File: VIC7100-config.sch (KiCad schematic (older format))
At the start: 45 parts, among them Q1 DMG1013UWQ-7, U13 VIC7100, U2 GD25LQ256DWIGR, U7 STM811RW16F, Y2 ABM8G-25.000MHZ-18-D2Y-T, Y3 ABM8G-27.000MHZ-18-D2Y-T

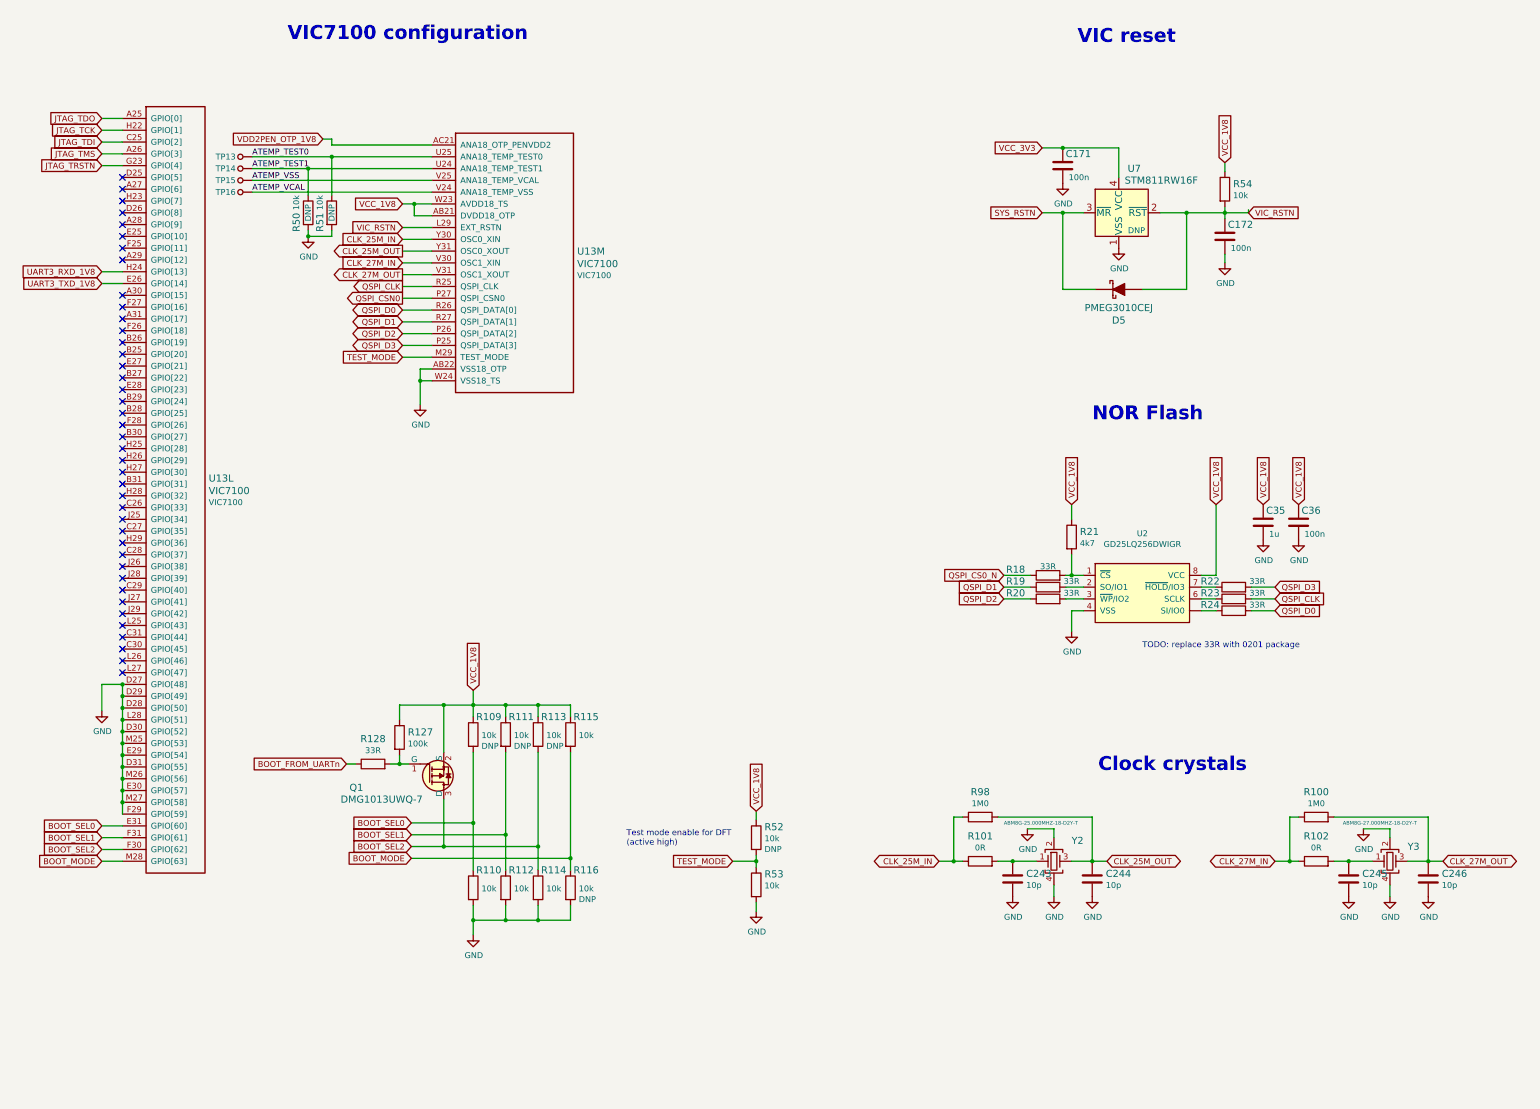
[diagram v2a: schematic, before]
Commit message: Added JTAG connector
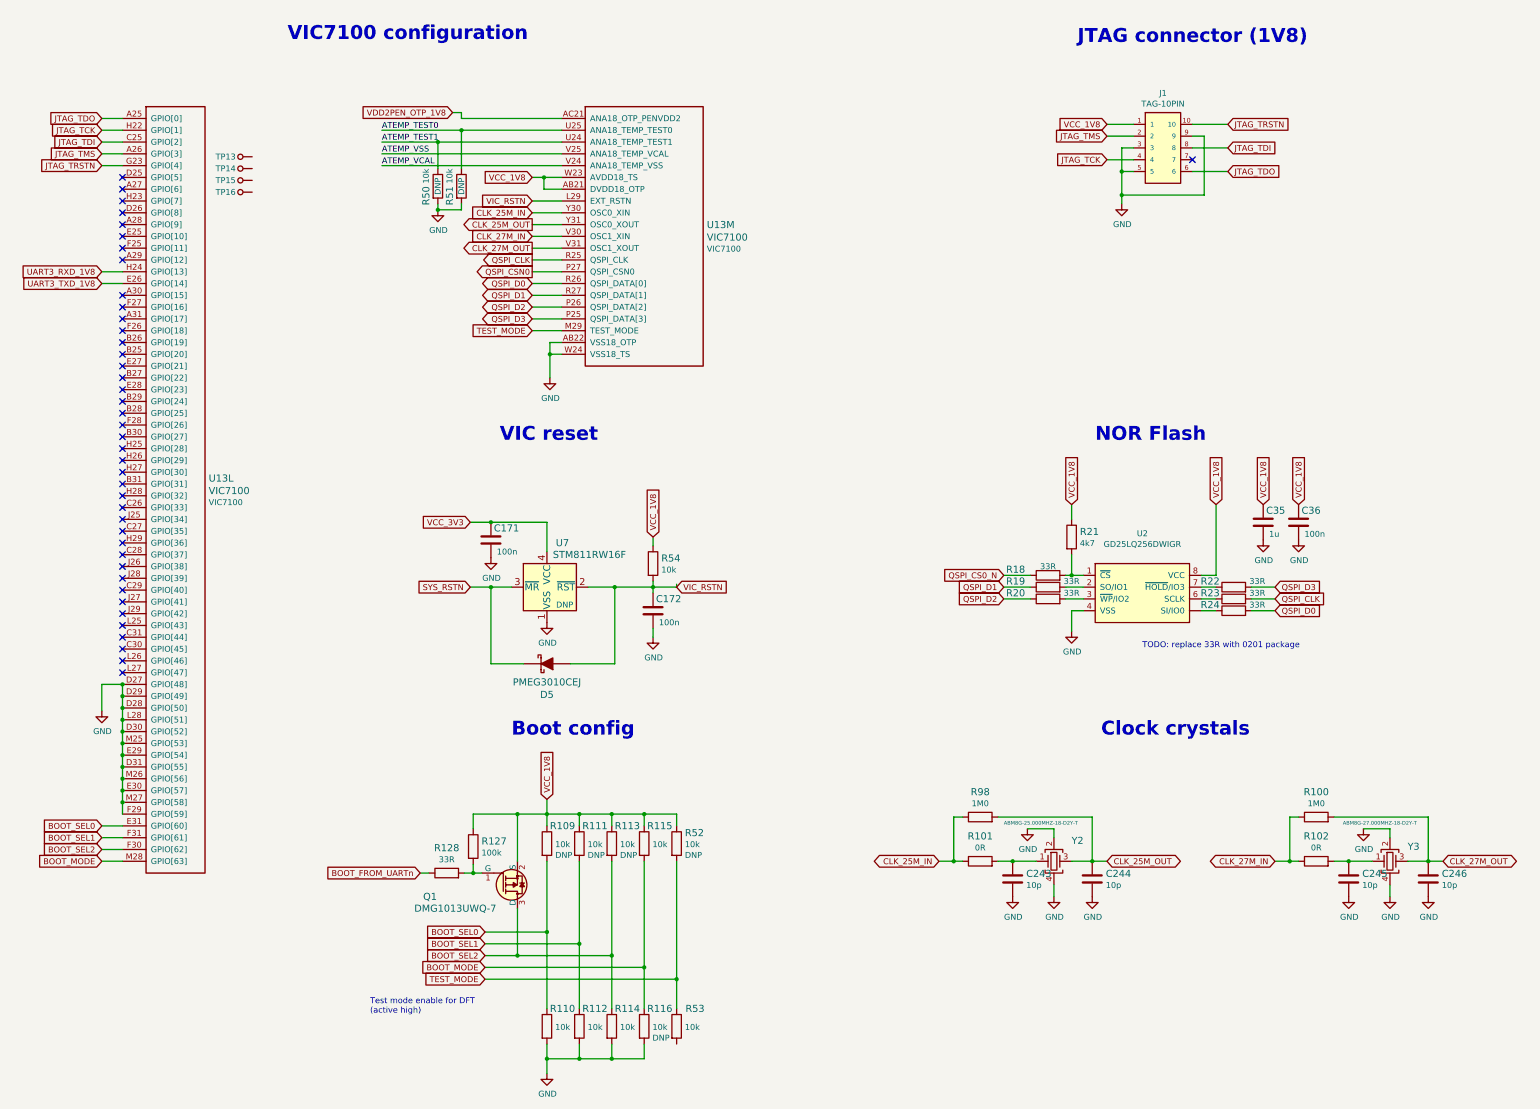
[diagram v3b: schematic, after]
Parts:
- added J1: TAG-10PIN, arvsom-footprints:Tag-Connect_TC2050-IDC-NL, symbol arvsom:TAG-10PIN
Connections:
- net ATEMP_TEST0: no longer TP13.1
- net ATEMP_TEST1: no longer TP14.1
- net ATEMP_VCAL: no longer TP16.1
- net ATEMP_VSS: no longer TP15.1
- net GND: now also J1.3, J1.5, J1.9; no longer R53.2
- net JTAG_TCK: now also J1.4
- net JTAG_TDI: now also J1.8
- net JTAG_TDO: now also J1.6
- net JTAG_TMS: now also J1.2
- net JTAG_TRSTN: now also J1.10
- net VCC_1V8: now also J1.1
- no-connect marks 41 -> 42
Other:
- note added: "Boot config"
- note added: "JTAG connector (1V8)"
- moved on the sheet: C171, C172, D5, Q1, R109, R110, R111, R112, R113, R114, R115, R116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

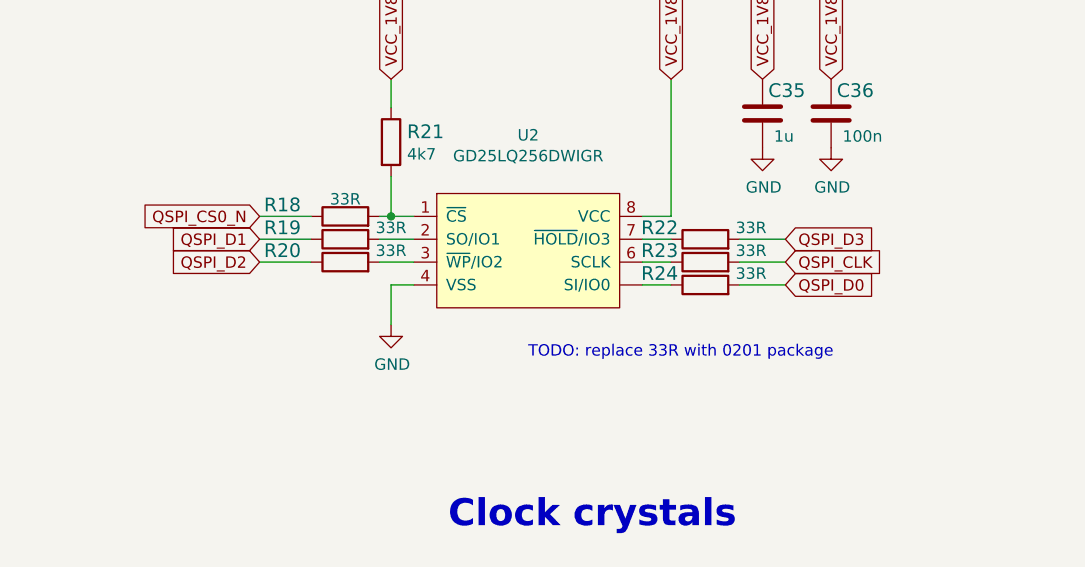
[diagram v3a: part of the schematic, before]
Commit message: Replaced 33R groups with resistor arrays
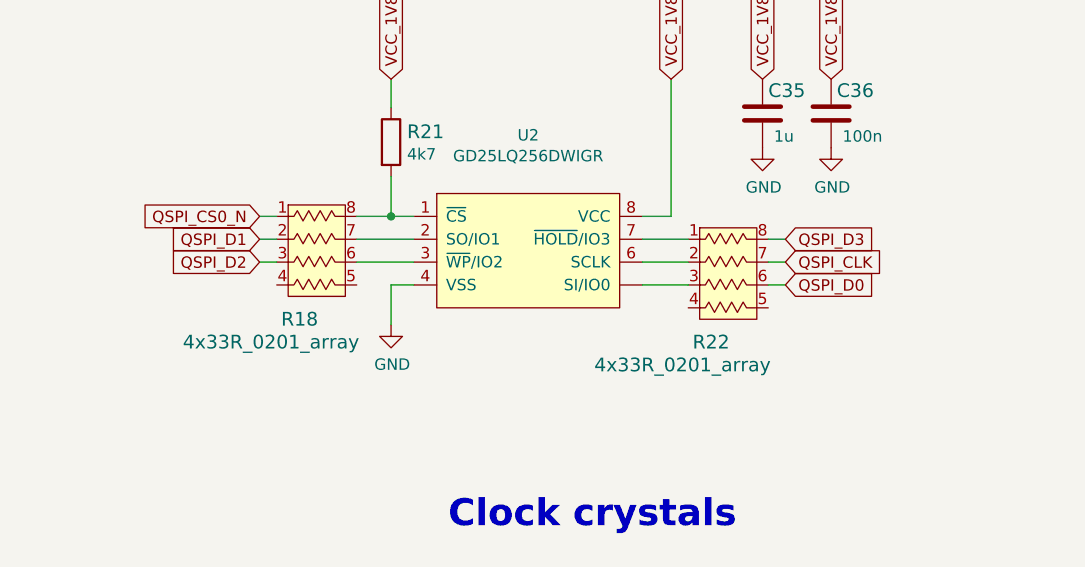
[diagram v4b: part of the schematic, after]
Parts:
- removed R18, R19, R20, R22, R23, R24: R_33R_0402, arvsom-footprints:0402-res, symbol arvsom:R_33R_0402
- added R18, R22: 4x33R_0201_array, arvsom-footprints:EXB18V, symbol arvsom:4x33R_0201_array
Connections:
- net QSPI_CLK: now also R22.7
- net QSPI_CS0_N: now also R18.1
- net QSPI_D0: now also R22.6
- net QSPI_D1: now also R18.2
- net QSPI_D2: now also R18.3
- net QSPI_D3: now also R22.8
- net at R21.2, U2.1 (~CS): now also R18.8
- net at U2.2 (SO/IO1): now also R18.7
- net at U2.3 (~WP~/IO2): now also R18.6
- net at U2.6 (SCLK): now also R22.2
- net at U2.7 (~HOLD~/IO3): now also R22.1
- net at U2.~ (SI/IO0): now also R22.3
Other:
- note removed: "TODO: replace 33R with 0201 package"
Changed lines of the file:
@@
 	1    0    0    -1
 $EndComp
-Wire Wire Line
-	11825 6425 11950 6425
-Wire Wire Line
-	11825 6225 11950 6225
-Wire Wire Line
-	10675 6225 10825 6225
-Wire Wire Line
-	10675 6325 10825 6325
-$Comp
-L arvsom:R_33R_0402 R?
-U 1 1 60ADDC73
-P 10525 6225
-AR Path="/607858CA/60ADDC73" Ref="R?"  Part="1"
-AR Path="/60805CC6/60ADDC73" Ref="R19"  Part="1"
-F 0 "R19" H 10250 6275 60  0000 C CNN
-F 1 "R_33R_0402" H 10525 6075 60  0001 C CNN
-F 2 "arvsom-footprints:0402-res" H 10725 6425 60  0001 L CNN
-F 3 "" H 10525 6225 50  0001 C CNN
-F 4 "Vishay" H 10725 6625 60  0001 L CNN "Manufacturer"
-F 5 "CRCW040233R0FKED" H 10725 6525 60  0001 L CNN "MPN"
-F 6 "33R" H 10725 6275 50  0000 C CNN "Val"
-	1    10525 6225
-	1    0    0    -1
-$EndComp
-$Comp
-L arvsom:R_33R_0402 R?
-U 1 1 60ADDC7C
-P 10525 6325
-AR Path="/607858CA/60ADDC7C" Ref="R?"  Part="1"
-AR Path="/60805CC6/60ADDC7C" Ref="R20"  Part="1"
-F 0 "R20" H 10250 6375 60  0000 C CNN
-F 1 "R_33R_0402" H 10525 6175 60  0001 C CNN
-F 2 "arvsom-footprints:0402-res" H 10725 6525 60  0001 L CNN
-F 3 "" H 10525 6325 50  0001 C CNN
-F 4 "Vishay" H 10725 6725 60  0001 L CNN "Manufacturer"
-F 5 "CRCW040233R0FKED" H 10725 6625 60  0001 L CNN "MPN"
-F 6 "33R" H 10725 6375 50  0000 C CNN "Val"
-	1    10525 6325
-	1    0    0    -1
-$EndComp
-$Comp
-L arvsom:R_33R_0402 R?
-U 1 1 60ADDC85
-P 12100 6225
-AR Path="/607858CA/60ADDC85" Ref="R?"  Part="1"
-AR Path="/60805CC6/60ADDC85" Ref="R22"  Part="1"
-F 0 "R22" H 11900 6275 60  0000 C CNN
-F 1 "R_33R_0402" H 12100 6075 60  0001 C CNN
-F 2 "arvsom-footprints:0402-res" H 12300 6425 60  0001 L CNN
-F 3 "" H 12100 6225 50  0001 C CNN
-F 4 "Vishay" H 12300 6625 60  0001 L CNN "Manufacturer"
-F 5 "CRCW040233R0FKED" H 12300 6525 60  0001 L CNN "MPN"
-F 6 "33R" H 12300 6275 50  0000 C CNN "Val"
-	1    12100 6225
-	1    0    0    -1
-$EndComp
-$Comp
-L arvsom:R_33R_0402 R?
-U 1 1 60ADDC8E
-P 12100 6425
-AR Path="/607858CA/60ADDC8E" Ref="R?"  Part="1"
-AR Path="/60805CC6/60ADDC8E" Ref="R24"  Part="1"
-F 0 "R24" H 11900 6475 60  0000 C CNN
-F 1 "R_33R_0402" H 12100 6275 60  0001 C CNN
-F 2 "arvsom-footprints:0402-res" H 12300 6625 60  0001 L CNN
-F 3 "" H 12100 6425 50  0001 C CNN
-F 4 "Vishay" H 12300 6825 60  0001 L CNN "Manufacturer"
-F 5 "CRCW040233R0FKED" H 12300 6725 60  0001 L CNN "MPN"
-F 6 "33R" H 12300 6475 50  0000 C CNN "Val"
-	1    12100 6425
-	1    0    0    -1
-$EndComp
-Wire Wire Line
-	12250 6225 12450 6225
-Wire Wire Line
-	12250 6425 12450 6425
-Wire Wire Line
-	10150 6225 10375 6225
-Wire Wire Line
-	10150 6325 10375 6325
 Text GLabel 10150 6225 0    50   Input ~ 0
 QSPI_D1
@@
 	1    0    0    -1
 $EndComp
-$Comp
-L arvsom:R_33R_0402 R?
-U 1 1 60ADDCCA
-P 12100 6325
-AR Path="/607858CA/60ADDCCA" Ref="R?"  Part="1"
-AR Path="/60805CC6/60ADDCCA" Ref="R23"  Part="1"
-F 0 "R23" H 11900 6375 60  0000 C CNN
-F 1 "R_33R_0402" H 12100 6175 60  0001 C CNN
-F 2 "arvsom-footprints:0402-res" H 12300 6525 60  0001 L CNN
-F 3 "" H 12100 6325 50  0001 C CNN
-F 4 "Vishay" H 12300 6725 60  0001 L CNN "Manufacturer"
-F 5 "CRCW040233R0FKED" H 12300 6625 60  0001 L CNN "MPN"
-F 6 "33R" H 12300 6375 50  0000 C CNN "Val"
-	1    12100 6325
-	1    0    0    -1
-$EndComp
-Wire Wire Line
-	11825 6325 11950 6325
-Wire Wire Line
-	12250 6325 12450 6325
 Text GLabel 12450 6325 2    50   Input ~ 0
 QSPI_CLK
@@
 	0    1    1    0
 $EndComp
-Wire Wire Line
-	10675 6125 10725 6125
-$Comp
-L arvsom:R_33R_0402 R?
-U 1 1 60ADDCE0
-P 10525 6125
-AR Path="/607858CA/60ADDCE0" Ref="R?"  Part="1"
-AR Path="/60805CC6/60ADDCE0" Ref="R18"  Part="1"
-F 0 "R18" H 10250 6175 60  0000 C CNN
-F 1 "R_33R_0402" H 10525 5975 60  0001 C CNN
-F 2 "arvsom-footprints:0402-res" H 10725 6325 60  0001 L CNN
-F 3 "" H 10525 6125 50  0001 C CNN
-F 4 "Vishay" H 10725 6525 60  0001 L CNN "Manufacturer"
-F 5 "CRCW040233R0FKED" H 10725 6425 60  0001 L CNN "MPN"
-F 6 "33R" H 10525 6200 50  0000 C CNN "Val"
-	1    10525 6125
-	1    0    0    -1
-$EndComp
-Wire Wire Line
-	10375 6125 10150 6125
 Text GLabel 10150 6125 0    50   Input ~ 0
 QSPI_CS0_N
@@
 Wire Wire Line
 	10725 6125 10825 6125
-Text Notes 11325 6750 0    50   ~ 0
-TODO: replace 33R with 0201 package
 Text Notes 4075 1600 0    118  ~ 24
 VIC7100 configuration
@@
 Wire Wire Line
 	11150 2700 11150 2900
+Wire Wire Line
+	10225 6125 10150 6125
+Wire Wire Line
+	10150 6225 10225 6225
+Wire Wire Line
+	10150 6325 10225 6325
+Wire Wire Line
+	10575 6125 10725 6125
+Wire Wire Line
+	10575 6225 10825 6225
+Wire Wire Line
+	10575 6325 10825 6325
+Wire Wire Line
+	12375 6325 12450 6325
+Wire Wire Line
+	12375 6425 12450 6425
+Wire Wire Line
+	12450 6225 12375 6225
+$Comp
+L arvsom:4x33R_0201_array R22
+U 1 1 609DE671
+P 12225 6625
+F 0 "R22" H 12125 6575 60  0000 C CNN
+F 1 "4x33R_0201_array" H 12000 6475 60  0000 C CNN
+F 2 "arvsom-footprints:EXB18V" H 12025 7375 60  0001 L CNN
+F 3 "http://industrial.panasonic.com/cdbs/www-data/pdf/AOC0000/AOC0000C14.pdf" H 12025 7375 60  0001 L CNN
+F 4 "EXB-18V330JX" H 12025 7575 60  0001 L CNN "MPN"
+F 5 "Panasonic" H 12025 7475 60  0001 L CNN "Manufacturer"
+	1    12225 6625
+	1    0    0    -1
+$EndComp
+Wire Wire Line
+	11825 6225 12025 6225
+Wire Wire Line
+	11825 6325 12025 6325
+Wire Wire Line
+	11825 6425 12025 6425
+$Comp
+L arvsom:4x33R_0201_array R18
+U 1 1 609A67A4
+P 10425 6525
+F 0 "R18" H 10325 6475 60  0000 C CNN
+F 1 "4x33R_0201_array" H 10200 6375 60  0000 C CNN
+F 2 "arvsom-footprints:EXB18V" H 10225 7275 60  0001 L CNN
+F 3 "http://industrial.panasonic.com/cdbs/www-data/pdf/AOC0000/AOC0000C14.pdf" H 10225 7275 60  0001 L CNN
+F 4 "EXB-18V330JX" H 10225 7475 60  0001 L CNN "MPN"
+F 5 "Panasonic" H 10225 7375 60  0001 L CNN "Manufacturer"
+	1    10425 6525
+	1    0    0    -1
+$EndComp
 $EndSCHEMATC
